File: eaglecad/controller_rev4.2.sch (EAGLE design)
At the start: 77 parts, among them U100 STM32L452XX_QFPN48, U101 TCAN330, U200 TPS63070, U300 STSPIN230, U301 TSV991ILT, U302 AS5047P, U400 STSPIN250, U401 TSV991ILT, X101 ABM10-16MHz

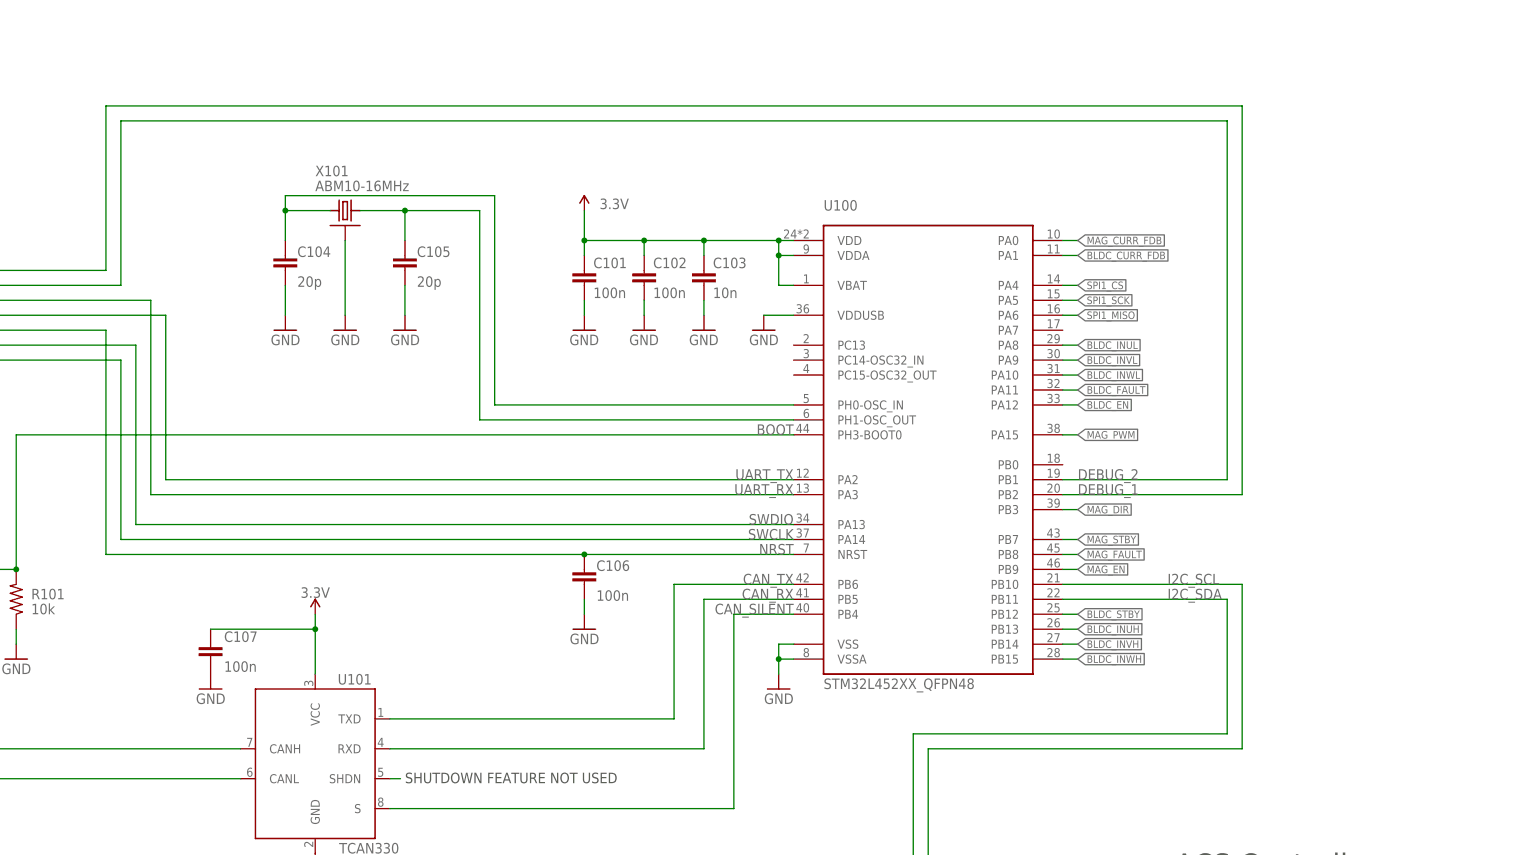
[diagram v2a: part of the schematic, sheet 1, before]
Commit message: added quadrent marker resistors and tappered lower corners for more clearence
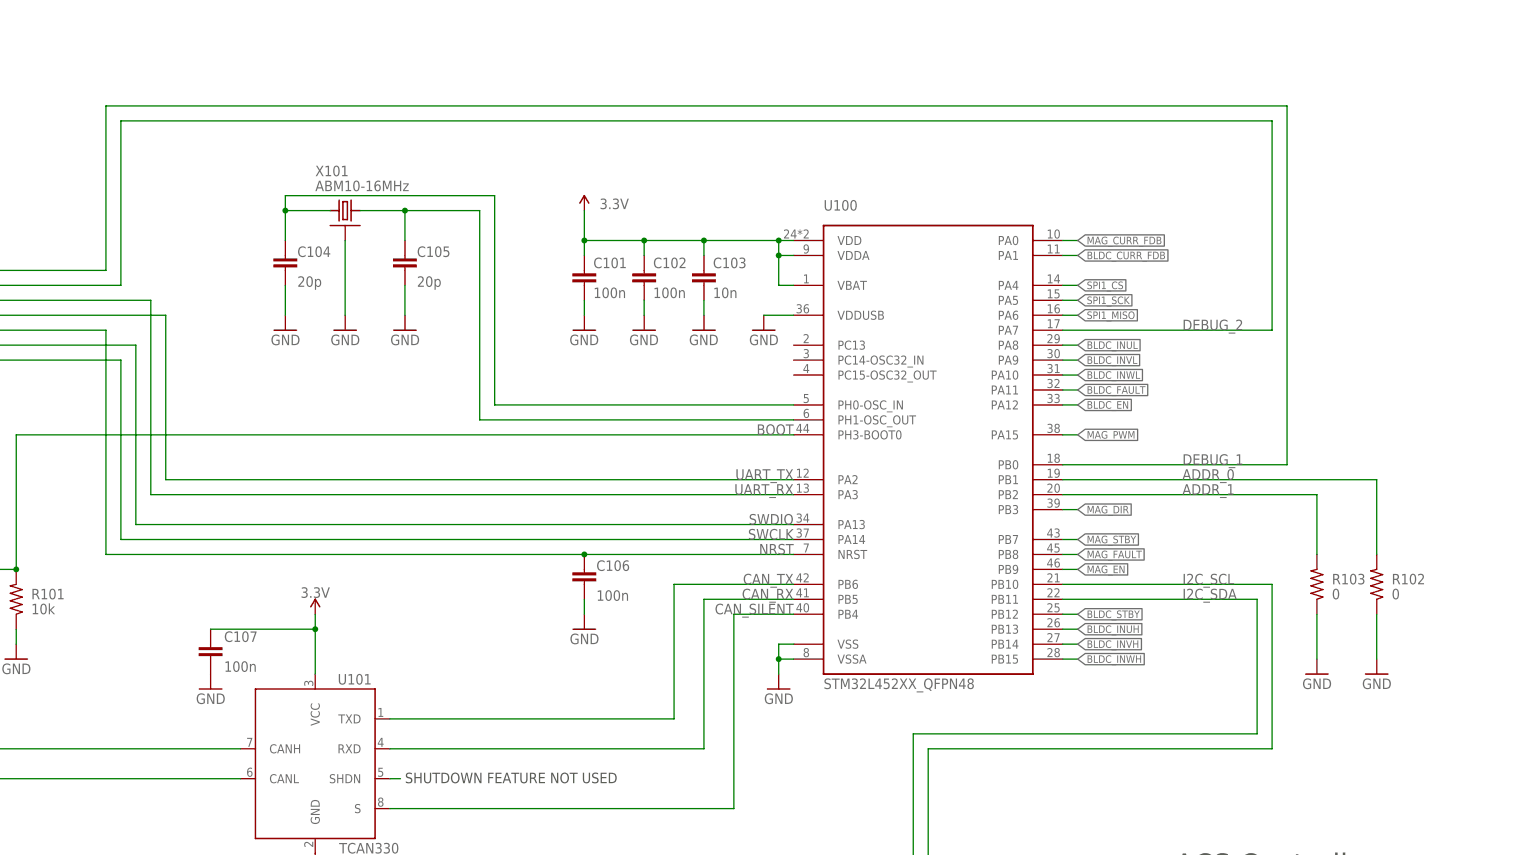
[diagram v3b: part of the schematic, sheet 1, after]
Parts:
- added R102, R103: 0, rcl_custom:R-US_0402-B-NOSILK
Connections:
- new net ADDR_0: R102.2, U100.PB1
- new net ADDR_1: R103.2, U100.PB2
- net DEBUG_1: now also U100.PB0; no longer U100.PB2
- net DEBUG_2: now also U100.PA7; no longer U100.PB1
- net GND: now also R102.1, R103.1
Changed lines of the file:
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@@
 <part name="GND17" library="supply1" deviceset="GND" device=""/>
 <part name="U$1" library="oresat-ACS_driver_board" deviceset="DRIVER-FLEX_CONN" device=""/>
+<part name="R103" library="rcl_custom" deviceset="R-US_" device="0402-B-NOSILK" value="0">
+<attribute name="DIS" value="Digi-Key"/>
+<attribute name="DPN" value="1276-4275-1-ND"/>
+<attribute name="MFR" value="Samsung"/>
+<attribute name="MPN" value="RC1005F6653CS"/>
+</part>
+<part name="R102" library="rcl_custom" deviceset="R-US_" device="0402-B-NOSILK" value="0">
+<attribute name="DIS" value="Digi-Key"/>
+<attribute name="DPN" value="1276-4275-1-ND"/>
+<attribute name="MFR" value="Samsung"/>
+<attribute name="MPN" value="RC1005F6653CS"/>
+</part>
+<part name="GND20" library="supply1" deviceset="GND" device=""/>
+<part name="GND22" library="supply1" deviceset="GND" device=""/>
 </parts>
 <sheets>
@@
 </instance>
 <instance part="U$1" gate="G$1" x="88.9" y="81.28" smashed="yes" rot="MR0"/>
+<instance part="R103" gate="R" x="365.76" y="76.2" smashed="yes" rot="MR90">
+<attribute name="DIS" x="365.76" y="76.2" size="1.778" layer="96" rot="MR90" display="off"/>
+<attribute name="DPN" x="365.76" y="76.2" size="1.778" layer="96" rot="MR90" display="off"/>
+<attribute name="MFR" x="365.76" y="76.2" size="1.778" layer="96" rot="MR90" display="off"/>
+<attribute name="MPN" x="365.76" y="76.2" size="1.778" layer="96" rot="MR90" display="off"/>
+<attribute name="NAME" x="368.3" y="76.2" size="1.778" layer="95"/>
+<attribute name="VALUE" x="368.3" y="73.66" size="1.778" layer="96"/>
+</instance>
+<instance part="R102" gate="R" x="375.92" y="76.2" smashed="yes" rot="MR90">
+<attribute name="DIS" x="375.92" y="76.2" size="1.778" layer="96" rot="MR90" display="off"/>
+<attribute name="DPN" x="375.92" y="76.2" size="1.778" layer="96" rot="MR90" display="off"/>
+<attribute name="MFR" x="375.92" y="76.2" size="1.778" layer="96" rot="MR90" display="off"/>
+<attribute name="MPN" x="375.92" y="76.2" size="1.778" layer="96" rot="MR90" display="off"/>
+<attribute name="NAME" x="378.46" y="76.2" size="1.778" layer="95"/>
+<attribute name="VALUE" x="378.46" y="73.66" size="1.778" layer="96"/>
+</instance>
+<instance part="GND20" gate="1" x="365.76" y="60.96" smashed="yes" rot="MR0">
+<attribute name="VALUE" x="368.3" y="58.42" size="1.778" layer="96" rot="MR0"/>
+</instance>
+<instance part="GND22" gate="1" x="375.92" y="60.96" smashed="yes" rot="MR0">
+<attribute name="VALUE" x="378.46" y="58.42" size="1.778" layer="96" rot="MR0"/>
+</instance>
 </instances>
 <busses>
@@
 <wire x1="88.9" y1="71.12" x2="92.964" y2="71.12" width="0.1524" layer="91"/>
 <wire x1="92.964" y1="71.12" x2="92.964" y2="67.31" width="0.1524" layer="91"/>
+</segment>
+<segment>
+<pinref part="R103" gate="R" pin="1"/>
+<pinref part="GND20" gate="1" pin="GND"/>
+<wire x1="365.76" y1="63.5" x2="365.76" y2="71.12" width="0.1524" layer="91"/>
+</segment>
+<segment>
+<pinref part="R102" gate="R" pin="1"/>
+<pinref part="GND22" gate="1" pin="GND"/>
+<wire x1="375.92" y1="63.5" x2="375.92" y2="71.12" width="0.1524" layer="91"/>
 </segment>
 </net>
@@
 <net name="DEBUG_2" class="0">
 <segment>
-<pinref part="U100" gate="G$1" pin="PB1"/>
-<label x="325.12" y="93.98" size="1.778" layer="95"/>
-<wire x1="322.58" y1="93.98" x2="350.52" y2="93.98" width="0.1524" layer="91"/>
-<wire x1="350.52" y1="93.98" x2="350.52" y2="154.94" width="0.1524" layer="91"/>
-<wire x1="350.52" y1="154.94" x2="162.56" y2="154.94" width="0.1524" layer="91"/>
+<label x="342.9" y="119.38" size="1.778" layer="95"/>
+<wire x1="358.14" y1="119.38" x2="358.14" y2="154.94" width="0.1524" layer="91"/>
+<wire x1="358.14" y1="154.94" x2="162.56" y2="154.94" width="0.1524" layer="91"/>
 <pinref part="C501" gate="G$1" pin="4"/>
 <wire x1="162.56" y1="154.94" x2="162.56" y2="127" width="0.1524" layer="91"/>
 <wire x1="162.56" y1="127" x2="87.884" y2="127" width="0.1524" layer="91"/>
+<pinref part="U100" gate="G$1" pin="PA7"/>
+<wire x1="358.14" y1="119.38" x2="322.58" y2="119.38" width="0.1524" layer="91"/>
 </segment>
 </net>
@@
 <wire x1="87.884" y1="129.54" x2="160.02" y2="129.54" width="0.1524" layer="91"/>
 <wire x1="160.02" y1="129.54" x2="160.02" y2="157.48" width="0.1524" layer="91"/>
-<wire x1="160.02" y1="157.48" x2="353.06" y2="157.48" width="0.1524" layer="91"/>
-<wire x1="353.06" y1="157.48" x2="353.06" y2="91.44" width="0.1524" layer="91"/>
-<pinref part="U100" gate="G$1" pin="PB2"/>
-<label x="325.12" y="91.44" size="1.778" layer="95"/>
-<wire x1="353.06" y1="91.44" x2="322.58" y2="91.44" width="0.1524" layer="91"/>
+<wire x1="160.02" y1="157.48" x2="360.68" y2="157.48" width="0.1524" layer="91"/>
+<wire x1="360.68" y1="157.48" x2="360.68" y2="96.52" width="0.1524" layer="91"/>
+<label x="342.9" y="96.52" size="1.778" layer="95"/>
+<pinref part="U100" gate="G$1" pin="PB0"/>
+<wire x1="360.68" y1="96.52" x2="322.58" y2="96.52" width="0.1524" layer="91"/>
 </segment>
 </net>
@@
 <segment>
 <pinref part="U100" gate="G$1" pin="PB10"/>
-<label x="340.36" y="76.2" size="1.778" layer="255"/>
-<wire x1="322.58" y1="76.2" x2="353.06" y2="76.2" width="0.1524" layer="91"/>
-<wire x1="353.06" y1="76.2" x2="353.06" y2="48.26" width="0.1524" layer="91"/>
-<wire x1="353.06" y1="48.26" x2="299.72" y2="48.26" width="0.1524" layer="91"/>
+<label x="342.9" y="76.2" size="1.778" layer="255"/>
+<wire x1="322.58" y1="76.2" x2="358.14" y2="76.2" width="0.1524" layer="91"/>
+<wire x1="358.14" y1="76.2" x2="358.14" y2="48.26" width="0.1524" layer="91"/>
+<wire x1="358.14" y1="48.26" x2="299.72" y2="48.26" width="0.1524" layer="91"/>
 <wire x1="299.72" y1="48.26" x2="299.72" y2="15.24" width="0.1524" layer="91"/>
 <wire x1="299.72" y1="15.24" x2="129.54" y2="15.24" width="0.1524" layer="91"/>
@@
 <segment>
 <pinref part="U100" gate="G$1" pin="PB11"/>
-<label x="340.36" y="73.66" size="1.778" layer="255"/>
-<wire x1="322.58" y1="73.66" x2="350.52" y2="73.66" width="0.1524" layer="91"/>
-<wire x1="350.52" y1="73.66" x2="350.52" y2="50.8" width="0.1524" layer="91"/>
-<wire x1="350.52" y1="50.8" x2="297.18" y2="50.8" width="0.1524" layer="91"/>
+<label x="342.9" y="73.66" size="1.778" layer="255"/>
+<wire x1="322.58" y1="73.66" x2="355.6" y2="73.66" width="0.1524" layer="91"/>
+<wire x1="355.6" y1="73.66" x2="355.6" y2="50.8" width="0.1524" layer="91"/>
+<wire x1="355.6" y1="50.8" x2="297.18" y2="50.8" width="0.1524" layer="91"/>
 <wire x1="297.18" y1="50.8" x2="297.18" y2="17.78" width="0.1524" layer="91"/>
 <wire x1="297.18" y1="17.78" x2="132.08" y2="17.78" width="0.1524" layer="91"/>
@@
 <wire x1="132.08" y1="17.78" x2="132.08" y2="81.28" width="0.1524" layer="91"/>
 <wire x1="132.08" y1="81.28" x2="88.9" y2="81.28" width="0.1524" layer="91"/>
+</segment>
+</net>
+<net name="ADDR_0" class="0">
+<segment>
+<pinref part="U100" gate="G$1" pin="PB1"/>
+<pinref part="R102" gate="R" pin="2"/>
+<wire x1="322.58" y1="93.98" x2="375.92" y2="93.98" width="0.1524" layer="91"/>
+<wire x1="375.92" y1="93.98" x2="375.92" y2="81.28" width="0.1524" layer="91"/>
+<label x="342.9" y="93.98" size="1.778" layer="95"/>
+</segment>
+</net>
+<net name="ADDR_1" class="0">
+<segment>
+<pinref part="U100" gate="G$1" pin="PB2"/>
+<wire x1="322.58" y1="91.44" x2="365.76" y2="91.44" width="0.1524" layer="91"/>
+<pinref part="R103" gate="R" pin="2"/>
+<wire x1="365.76" y1="91.44" x2="365.76" y2="81.28" width="0.1524" layer="91"/>
+<label x="342.9" y="91.44" size="1.778" layer="95"/>
 </segment>
 </net>
@@
 </instance>
 <instance part="FRAME3" gate="G$1" x="0" y="0" smashed="yes"/>
-<instance part="FRAME3" gate="G$2" x="327.66" y="0" smashed="yes">
-<attribute name="LAST_DATE_TIME" x="340.36" y="1.27" size="2.54" layer="94"/>
-<attribute name="SHEET" x="414.02" y="1.27" size="2.54" layer="94"/>
-<attribute name="DRAWING_NAME" x="342.9" y="19.05" size="2.54" layer="97"/>
+<instance part="FRAME3" gate="G$2" x="325.12" y="0" smashed="yes">
+<attribute name="LAST_DATE_TIME" x="337.82" y="1.27" size="2.54" layer="94"/>
+<attribute name="SHEET" x="411.48" y="1.27" size="2.54" layer="94"/>
+<attribute name="DRAWING_NAME" x="340.36" y="19.05" size="2.54" layer="97"/>
 </instance>
 <instance part="SUPPLY18" gate="G$1" x="243.84" y="147.32" smashed="yes" rot="MR0">
